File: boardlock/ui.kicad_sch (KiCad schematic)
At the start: 37 parts, among them J6 USB_C_Receptacle_USB2.0, Q5 MMBT4401, Q6 MMBT4401, Q7 MMBT4401, SW1 SW_Push, SW2 SW_Push, U9 TPD2E2U06

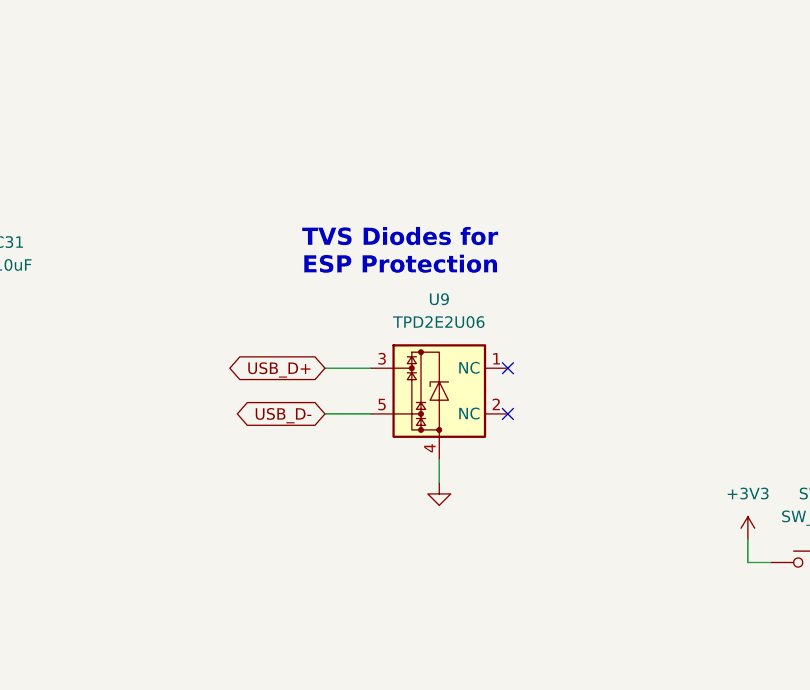
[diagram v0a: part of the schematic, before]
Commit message: started on boost converter
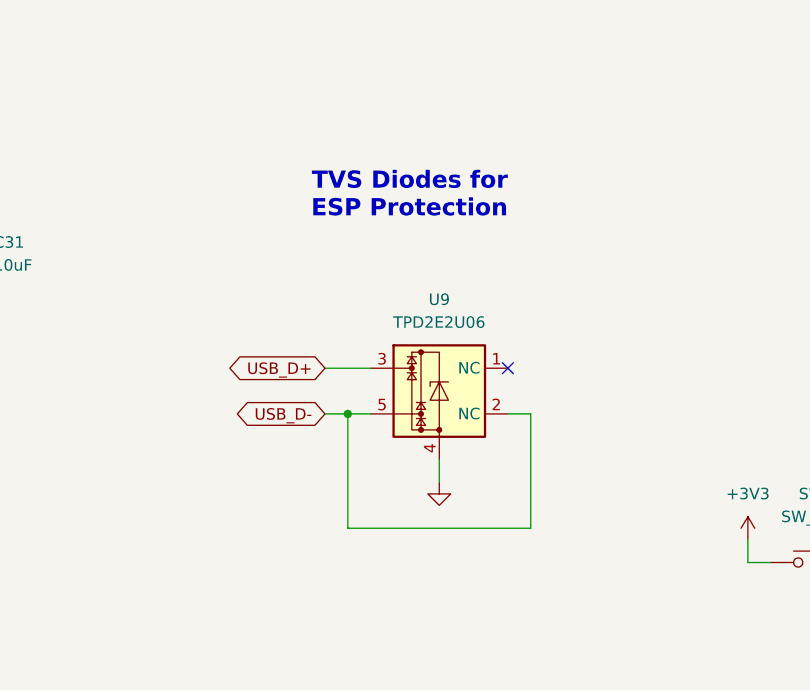
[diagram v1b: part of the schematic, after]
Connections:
- net USB_D-: now also U9.2 (NC)
- no-connect marks 4 -> 3
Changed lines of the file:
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@@
   (junction (at 265.43 85.09) (diameter 0) (color 0 0 0 0)
   )
+  (junction (at 133.35 68.58) (diameter 0) (color 0 0 0 0)
+  )
   (junction (at 205.74 92.71) (diameter 0) (color 0 0 0 0)
   )
@@
   (junction (at 142.24 170.18) (diameter 0) (color 0 0 0 0)
   )
-  (no_connect (at 151.13 68.58))
   (no_connect (at 62.23 73.66))
   (no_connect (at 62.23 76.2))
@@
     (stroke (width 0) (type default))
   )
+  (wire (pts (xy 130.81 63.5) (xy 135.89 63.5))
+    (stroke (width 0) (type default))
+  )
   (wire (pts (xy 200.66 116.84) (xy 200.66 115.57))
     (stroke (width 0) (type default))
@@
     (stroke (width 0) (type default))
   )
-  (wire (pts (xy 130.81 63.5) (xy 135.89 63.5))
-    (stroke (width 0) (type default))
-  )
   (wire (pts (xy 234.95 85.09) (xy 232.41 85.09))
     (stroke (width 0) (type default))
   )
+  (wire (pts (xy 133.35 81.28) (xy 153.67 81.28))
+    (stroke (width 0) (type default))
+  )
   (wire (pts (xy 234.95 40.64) (xy 234.95 41.91))
     (stroke (width 0) (type default))
@@
     (stroke (width 0) (type default))
   )
+  (wire (pts (xy 153.67 68.58) (xy 151.13 68.58))
+    (stroke (width 0) (type default))
+  )
   (wire (pts (xy 66.04 68.58) (xy 66.04 66.04))
     (stroke (width 0) (type default))
@@
     (stroke (width 0) (type default))
   )
+  (wire (pts (xy 133.35 68.58) (xy 135.89 68.58))
+    (stroke (width 0) (type default))
+  )
   (wire (pts (xy 260.35 92.71) (xy 255.27 92.71))
     (stroke (width 0) (type default))
@@
     (stroke (width 0) (type default))
   )
+  (wire (pts (xy 133.35 68.58) (xy 133.35 81.28))
+    (stroke (width 0) (type default))
+  )
   (wire (pts (xy 133.35 160.02) (xy 134.62 160.02))
     (stroke (width 0) (type default))
@@
     (stroke (width 0) (type default))
   )
+  (wire (pts (xy 153.67 81.28) (xy 153.67 68.58))
+    (stroke (width 0) (type default))
+  )
   (wire (pts (xy 142.24 143.51) (xy 142.24 146.05))
     (stroke (width 0) (type default))
@@
     (stroke (width 0) (type default))
   )
-  (wire (pts (xy 130.81 68.58) (xy 135.89 68.58))
+  (wire (pts (xy 130.81 68.58) (xy 133.35 68.58))
     (stroke (width 0) (type default))
   )
@@
     (effects (font (size 1.27 1.27) bold) (justify left bottom))
   )
-  (text "TVS Diodes for\nESP Protection" (at 128.27 53.34 0)
-    (effects (font (size 1.905 1.905) (thickness 0.381) bold) (justify left bottom))
+  (text "TVS Diodes for\nESP Protection" (at 151.13 46.99 0)
+    (effects (font (size 1.905 1.905) (thickness 0.381) bold) (justify right bottom))
   )
   (text "uC dev kit \nhas 2 caps" (at 201.93 49.53 0)

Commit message: led changes
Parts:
- removed Q5, Q6, Q7: MMBT4401, Package_TO_SOT_SMD:SOT-23-3, symbol Simulation_SPICE:NPN
- removed R54, R55, R56, R57, R58, R59: R_US, Resistor_SMD:R_0805_2012Metric_Pad1.20x1.40mm_HandSolder, symbol Device:R_US
- added Q5, Q6, Q7: DTC124X, Package_TO_SOT_SMD:SOT-23_Handsoldering, symbol Transistor_BJT:DTC124X
- R51: value R_US -> 12
- R52, R53: value R_US -> 5.6
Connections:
- net GND: now also Q5.1 (B), Q5.2 (E), Q6.1 (B), Q6.2 (E), Q7.1 (B), Q7.2 (E)
- net at R52.2: now also Q6.3 (C)
- net at R51.2: now also Q5.3 (C)
- net at R53.2: now also Q7.3 (C)
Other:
- moved on the sheet: R51, R53

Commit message: buck-boost complete
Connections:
- net GND: no longer Q5.1 (B), Q6.1 (B), Q7.1 (B)
- new net M_RGB_B: Q7.1 (B)
- new net M_RGB_G: Q6.1 (B)
- new net M_RGB_R: Q5.1 (B)
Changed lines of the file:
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@@
   (junction (at 133.35 68.58) (diameter 0) (color 0 0 0 0)
   )
-  (junction (at 62.23 165.1) (diameter 0) (color 0 0 0 0)
-  )
   (junction (at 205.74 92.71) (diameter 0) (color 0 0 0 0)
   )
   (junction (at 205.74 116.84) (diameter 0) (color 0 0 0 0)
   )
-  (junction (at 123.19 158.75) (diameter 0) (color 0 0 0 0)
-  )
   (junction (at 200.66 40.64) (diameter 0) (color 0 0 0 0)
   )
   (junction (at 90.17 45.72) (diameter 0) (color 0 0 0 0)
   )
-  (junction (at 133.35 165.1) (diameter 0) (color 0 0 0 0)
-  )
   (junction (at 39.37 85.09) (diameter 0) (color 0 0 0 0)
   )
@@
   (junction (at 81.28 55.88) (diameter 0) (color 0 0 0 0)
   )
-  (junction (at 97.79 165.1) (diameter 0) (color 0 0 0 0)
-  )
   (junction (at 234.95 40.64) (diameter 0) (color 0 0 0 0)
   )
-  (junction (at 52.07 158.75) (diameter 0) (color 0 0 0 0)
-  )
   (junction (at 210.82 85.09) (diameter 0) (color 0 0 0 0)
   )
@@
   )
   (junction (at 255.27 85.09) (diameter 0) (color 0 0 0 0)
-  )
-  (junction (at 87.63 158.75) (diameter 0) (color 0 0 0 0)
   )
   (no_connect (at 62.23 73.66))
@@
     (stroke (width 0) (type default))
   )
-  (wire (pts (xy 50.8 158.75) (xy 52.07 158.75))
+  (wire (pts (xy 50.8 158.75) (xy 53.34 158.75))
     (stroke (width 0) (type default))
   )
@@
     (stroke (width 0) (type default))
   )
-  (wire (pts (xy 52.07 158.75) (xy 52.07 165.1))
-    (stroke (width 0) (type default))
-  )
   (wire (pts (xy 254 85.09) (xy 255.27 85.09))
     (stroke (width 0) (type default))
@@
     (stroke (width 0) (type default))
   )
-  (wire (pts (xy 52.07 158.75) (xy 53.34 158.75))
-    (stroke (width 0) (type default))
-  )
   (wire (pts (xy 234.95 85.09) (xy 232.41 85.09))
     (stroke (width 0) (type default))
@@
     (stroke (width 0) (type default))
   )
-  (wire (pts (xy 52.07 165.1) (xy 62.23 165.1))
-    (stroke (width 0) (type default))
-  )
   (wire (pts (xy 234.95 40.64) (xy 234.95 41.91))
     (stroke (width 0) (type default))
@@
     (stroke (width 0) (type default))
   )
-  (wire (pts (xy 123.19 158.75) (xy 123.19 165.1))
-    (stroke (width 0) (type default))
-  )
-  (wire (pts (xy 123.19 165.1) (xy 133.35 165.1))
-    (stroke (width 0) (type default))
-  )
   (wire (pts (xy 39.37 85.09) (xy 39.37 86.36))
     (stroke (width 0) (type default))
   )
-  (wire (pts (xy 133.35 163.83) (xy 133.35 165.1))
-    (stroke (width 0) (type default))
-  )
-  (wire (pts (xy 97.79 163.83) (xy 97.79 165.1))
-    (stroke (width 0) (type default))
-  )
   (wire (pts (xy 200.66 46.99) (xy 200.66 48.26))
     (stroke (width 0) (type default))
@@
     (stroke (width 0) (type default))
   )
-  (wire (pts (xy 87.63 158.75) (xy 87.63 165.1))
-    (stroke (width 0) (type default))
-  )
   (wire (pts (xy 232.41 40.64) (xy 234.95 40.64))
     (stroke (width 0) (type default))
   )
-  (wire (pts (xy 62.23 165.1) (xy 62.23 166.37))
+  (wire (pts (xy 62.23 163.83) (xy 62.23 166.37))
     (stroke (width 0) (type default))
   )
@@
     (stroke (width 0) (type default))
   )
-  (wire (pts (xy 123.19 158.75) (xy 124.46 158.75))
-    (stroke (width 0) (type default))
-  )
-  (wire (pts (xy 133.35 165.1) (xy 133.35 166.37))
+  (wire (pts (xy 121.92 158.75) (xy 124.46 158.75))
+    (stroke (width 0) (type default))
+  )
+  (wire (pts (xy 133.35 163.83) (xy 133.35 166.37))
     (stroke (width 0) (type default))
   )
@@
     (stroke (width 0) (type default))
   )
-  (wire (pts (xy 62.23 163.83) (xy 62.23 165.1))
-    (stroke (width 0) (type default))
-  )
-  (wire (pts (xy 87.63 165.1) (xy 97.79 165.1))
-    (stroke (width 0) (type default))
-  )
   (wire (pts (xy 97.79 143.51) (xy 97.79 144.78))
     (stroke (width 0) (type default))
@@
     (stroke (width 0) (type default))
   )
-  (wire (pts (xy 87.63 158.75) (xy 88.9 158.75))
+  (wire (pts (xy 86.36 158.75) (xy 88.9 158.75))
     (stroke (width 0) (type default))
   )
@@
     (stroke (width 0) (type default))
   )
-  (wire (pts (xy 97.79 165.1) (xy 97.79 166.37))
+  (wire (pts (xy 97.79 163.83) (xy 97.79 166.37))
     (stroke (width 0) (type default))
   )
@@
     (stroke (width 0) (type default))
   )
-  (wire (pts (xy 121.92 158.75) (xy 123.19 158.75))
-    (stroke (width 0) (type default))
-  )
   (wire (pts (xy 180.34 109.22) (xy 177.8 109.22))
     (stroke (width 0) (type default))
   )
-  (wire (pts (xy 86.36 158.75) (xy 87.63 158.75))
-    (stroke (width 0) (type default))
-  )

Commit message: some changes
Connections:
- net USB_D-: now also U9.1 (NC); no longer U9.2 (NC)
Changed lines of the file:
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@@
   (junction (at 255.27 85.09) (diameter 0) (color 0 0 0 0)
   )
+  (no_connect (at 151.13 68.58))
   (no_connect (at 62.23 73.66))
   (no_connect (at 62.23 76.2))
-  (no_connect (at 151.13 63.5))
   (wire (pts (xy 200.66 85.09) (xy 210.82 85.09))
     (stroke (width 0) (type default))
@@
     (stroke (width 0) (type default))
   )
-  (wire (pts (xy 153.67 68.58) (xy 151.13 68.58))
-    (stroke (width 0) (type default))
-  )
   (wire (pts (xy 66.04 68.58) (xy 66.04 66.04))
     (stroke (width 0) (type default))
@@
     (stroke (width 0) (type default))
   )
+  (wire (pts (xy 153.67 63.5) (xy 151.13 63.5))
+    (stroke (width 0) (type default))
+  )
   (wire (pts (xy 62.23 144.78) (xy 62.23 143.51))
     (stroke (width 0) (type default))
@@
     (stroke (width 0) (type default))
   )
-  (wire (pts (xy 153.67 81.28) (xy 153.67 68.58))
-    (stroke (width 0) (type default))
-  )
+  (wire (pts (xy 153.67 63.5) (xy 153.67 81.28))
+    (stroke (width 0) (type default))
+  )

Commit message: button and power fixes
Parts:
- removed SW1 (x2): SW_Push, TL3300DF160Q:SW_TL3300DF160Q, symbol Switch:SW_Push
- added SW3, SW5: TL3300DF160Q, TL3300DF160Q:SW_TL3300DF160Q, symbol TL3300DF160Q:TL3300DF160Q
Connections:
- net +3V3: now also SW3.1, SW5.1
- net at R49.1: now also SW5.3
- net at R45.1: now also SW3.3
- no-connect marks 3 -> 7

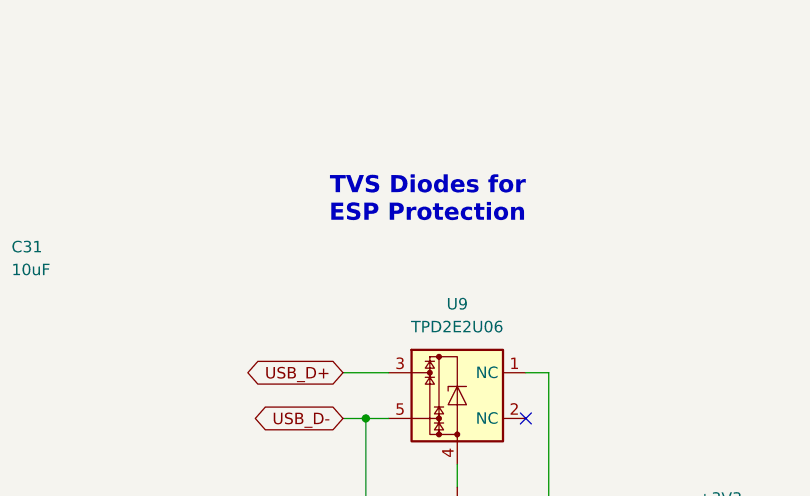
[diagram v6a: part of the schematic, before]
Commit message: added some GND vias
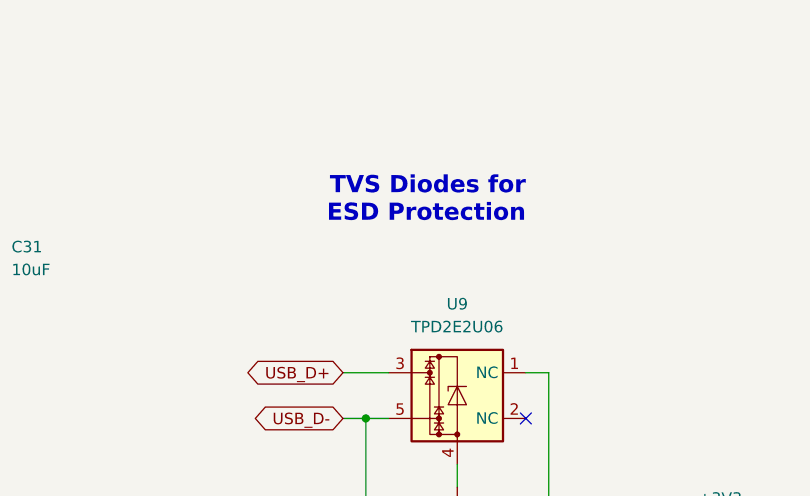
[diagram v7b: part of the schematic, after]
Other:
- note added: "TVS Diodes for ESD Protection"
- note removed: "TVS Diodes for ESP Protection"
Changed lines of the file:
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@@
     (effects (font (size 1.27 1.27) bold) (justify left bottom))
   )
-  (text "TVS Diodes for\nESP Protection" (at 151.13 46.99 0)
+  (text "TVS Diodes for\nESD Protection" (at 151.13 46.99 0)
     (effects (font (size 1.905 1.905) (thickness 0.381) bold) (justify right bottom))
   )

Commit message: small edits
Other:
- note removed: "check other circuitry in dev kit schematic to see if it's needed for RST and BOOT"
- note removed: "is boot typically high"
- note removed: "uC dev kit has 2 caps"
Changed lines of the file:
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@@
     (effects (font (size 1.905 1.905) (thickness 0.381) bold) (justify right bottom))
-  )
-  (text "uC dev kit \nhas 2 caps" (at 201.93 49.53 0)
-    (effects (font (size 1.27 1.27)) (justify left bottom))
   )
   (text "USB-C Connector\nin USB 2.0 Mode" (at 33.02 33.02 0)
     (effects (font (size 2.5 2.5) (thickness 0.5) bold) (justify left bottom))
   )
-  (text "is boot typically high" (at 238.76 48.26 0)
-    (effects (font (size 1.27 1.27) bold) (justify left bottom))
-  )
-  (text "check other circuitry in dev kit schematic to see if \nit's needed for RST and BOOT"
-    (at 194.31 59.69 0)
-    (effects (font (size 1.27 1.27)) (justify left bottom))
-  )
   (text "When laying out USB:\n1) Match trace length\n2) Keep same distance between traces"
